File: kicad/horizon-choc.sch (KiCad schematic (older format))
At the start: 96 parts, among them J1 OLED, SW1 SW_Push, SW10 SW_Push, SW11 SW_Push, SW12 SW_Push, SW13 SW_Push, SW14 SW_Push, SW15 SW_Push, SW16 SW_Push, SW17 SW_Push, SW18 SW_Push, SW19 SW_Push, SW2 SW_Push, SW20 SW_Push, SW21 SW_Push, SW22 SW_Push, SW23 SW_Push, SW24 SW_Push, SW25 SW_Push, SW26 SW_Push, SW27 SW_Push, SW28 SW_Push, SW29 SW_Push, SW3 SW_Push, SW30 SW_Push, SW31 SW_Push, SW32 SW_Push, SW33 SW_Push, SW34 SW_Push, SW35 SW_Push, SW36 SW_Push, SW37 SW_Push, SW38 SW_Push, SW39 SW_Push, SW4 SW_Push, SW40 SW_Push, SW41 SW_Push, SW42 SW_Push, SW5 SW_Push, SW6 SW_Push, SW7 SW_Push, SW8 SW_Push, SW9 SW_Push, U1 PRO-MICRO

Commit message: Adjust center component layout for MX and Choc consistency.
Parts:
- SW1, SW10, SW11, SW12, SW13, SW14, SW15, SW16, SW17, SW18, SW19, SW2, SW20, SW21, SW22, SW23, SW24, SW25, SW26, SW27, SW28, SW29, SW3, SW30, SW31, SW32, SW33, SW34, SW35, SW36, SW37, SW38, SW39, SW4, SW40, SW41, SW42, SW5, SW6, SW7, SW8, SW9: footprint horizon-footprints:SW_MX -> horizon-footprints:SW_Choc

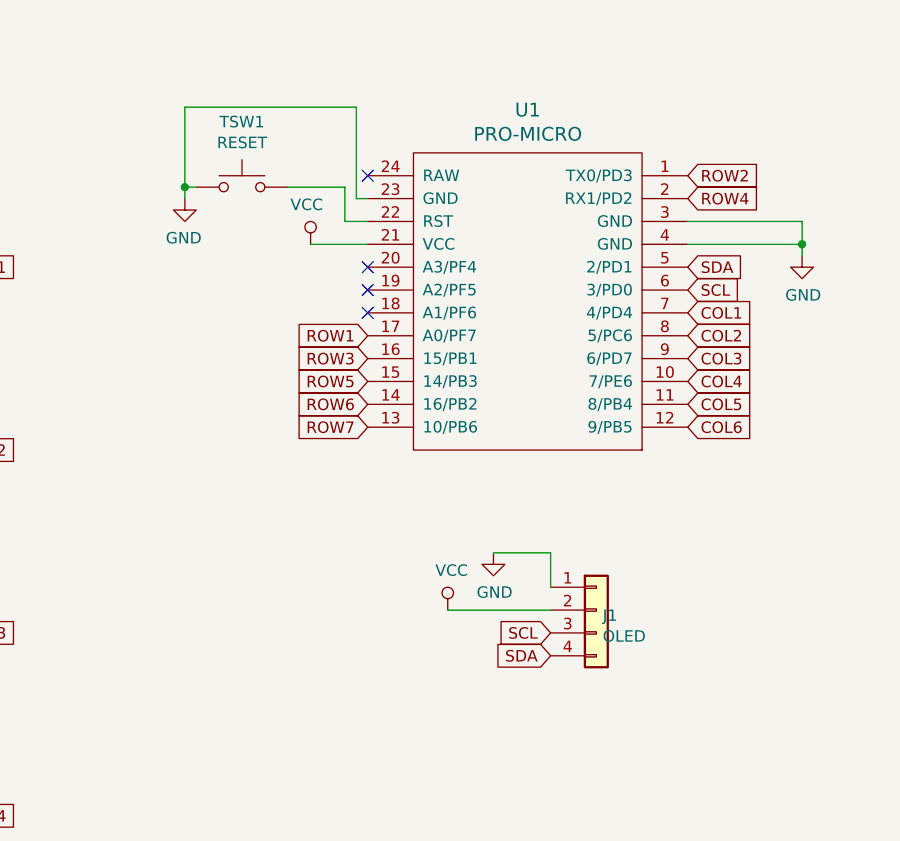
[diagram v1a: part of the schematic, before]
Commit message: Route traces on choc version
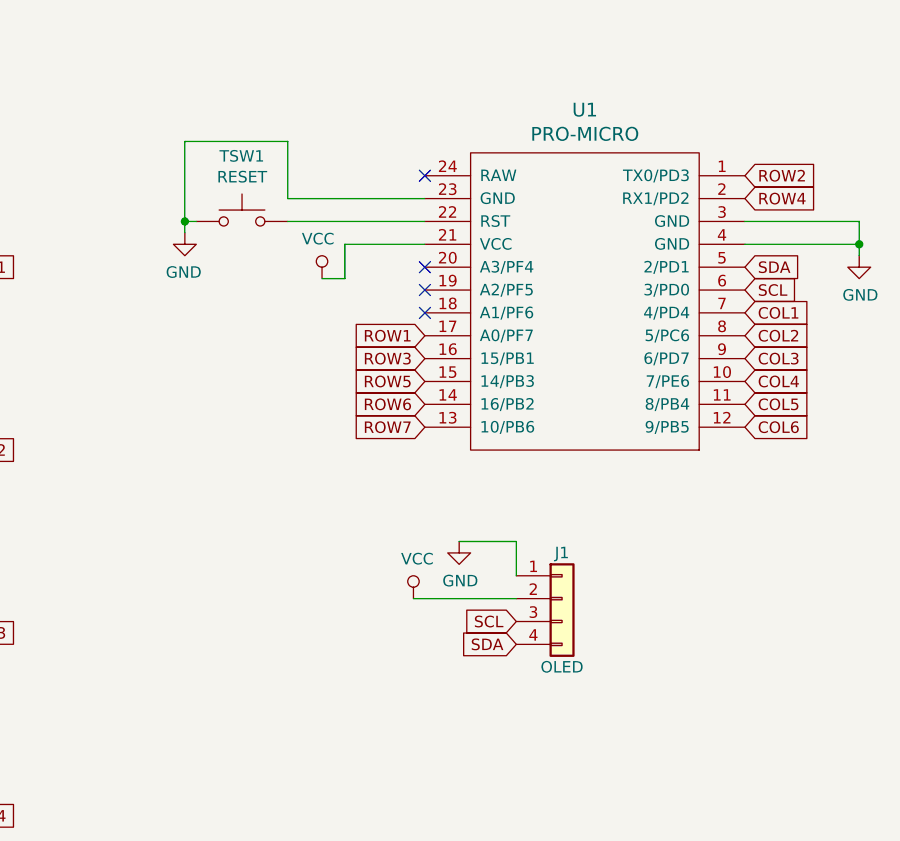
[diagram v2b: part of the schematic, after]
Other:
- moved on the sheet: J1, TSW1, U1
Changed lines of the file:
@@
 	1    0    0    -1
 $EndComp
-NoConn ~ 7800 1800
-Text GLabel 9200 2300 2    50   Input ~ 0
+NoConn ~ 8050 1800
+Text GLabel 9450 2300 2    50   Input ~ 0
 COL4
-Text GLabel 9200 1400 2    50   Input ~ 0
+Text GLabel 9450 1400 2    50   Input ~ 0
 ROW2
-Text GLabel 7800 2500 0    50   Input ~ 0
+Text GLabel 8050 2500 0    50   Input ~ 0
 ROW7
-Text GLabel 7800 2400 0    50   Input ~ 0
+Text GLabel 8050 2400 0    50   Input ~ 0
 ROW6
-Text GLabel 7800 2300 0    50   Input ~ 0
+Text GLabel 8050 2300 0    50   Input ~ 0
 ROW5
-Text GLabel 9200 1500 2    50   Input ~ 0
+Text GLabel 9450 1500 2    50   Input ~ 0
 ROW4
-Text GLabel 7800 2100 0    50   Input ~ 0
+Text GLabel 8050 2100 0    50   Input ~ 0
 ROW1
-Text GLabel 7800 2200 0    50   Input ~ 0
+Text GLabel 8050 2200 0    50   Input ~ 0
 ROW3
-Text GLabel 9200 2500 2    50   Input ~ 0
+Text GLabel 9450 2500 2    50   Input ~ 0
 COL6
-Text GLabel 9200 2400 2    50   Input ~ 0
+Text GLabel 9450 2400 2    50   Input ~ 0
 COL5
-Text GLabel 9200 2200 2    50   Input ~ 0
+Text GLabel 9450 2200 2    50   Input ~ 0
 COL3
-Text GLabel 9200 2100 2    50   Input ~ 0
+Text GLabel 9450 2100 2    50   Input ~ 0
 COL2
-Text GLabel 9200 2000 2    50   Input ~ 0
+Text GLabel 9450 2000 2    50   Input ~ 0
 COL1
 $Comp
 L horizon-components:Pro-Micro U1
 U 1 1 60FAFA60
-P 8500 1950
-F 0 "U1" H 8500 2787 60  0000 C CNN
-F 1 "PRO-MICRO" H 8500 2681 60  0000 C CNN
-F 2 "horizon-footprints:Pro-Micro" V 9550 -550 60  0001 C CNN
-F 3 "" V 9550 -550 60  0001 C CNN
-	1    8500 1950
+P 8750 1950
+F 0 "U1" H 8750 2787 60  0000 C CNN
+F 1 "PRO-MICRO" H 8750 2681 60  0000 C CNN
+F 2 "horizon-footprints:Pro-Micro" V 9800 -550 60  0001 C CNN
+F 3 "" V 9800 -550 60  0001 C CNN
+	1    8750 1950
 	-1   0    0    -1
 $EndComp
@@
 $EndComp
 NoConn ~ 9050 4550
-Text GLabel 8600 3500 0    50   Input ~ 0
+Text GLabel 8450 3450 0    50   Input ~ 0
 SDA
-Text GLabel 8600 3400 0    50   Input ~ 0
+Text GLabel 8450 3350 0    50   Input ~ 0
 SCL
 Wire Wire Line
-	8600 3050 8350 3050
-Wire Wire Line
-	8600 3200 8600 3050
-Wire Wire Line
-	8150 3300 8600 3300
+	8450 3000 8200 3000
+Wire Wire Line
+	8450 3150 8450 3000
+Wire Wire Line
+	8000 3250 8450 3250
 $Comp
 L power:VCC #PWR0105
 U 1 1 61061E80
-P 8150 3300
-F 0 "#PWR0105" H 8150 3150 50  0001 C CNN
-F 1 "VCC" H 8167 3473 50  0000 C CNN
-F 2 "" H 8150 3300 50  0001 C CNN
-F 3 "" H 8150 3300 50  0001 C CNN
-	1    8150 3300
-	1    0    0    -1
-$EndComp
-Wire Wire Line
-	7750 1100 7000 1100
-Wire Wire Line
-	7750 1100 7750 1500
-Wire Wire Line
-	7700 1600 7700 1450
-Wire Wire Line
-	7800 1600 7700 1600
-Wire Wire Line
-	7800 1700 7550 1700
+P 8000 3250
+F 0 "#PWR0105" H 8000 3100 50  0001 C CNN
+F 1 "VCC" H 8017 3423 50  0000 C CNN
+F 2 "" H 8000 3250 50  0001 C CNN
+F 3 "" H 8000 3250 50  0001 C CNN
+	1    8000 3250
+	1    0    0    -1
+$EndComp
+Text GLabel 9450 1900 2    50   Input ~ 0
+SCL
+Text GLabel 9450 1800 2    50   Input ~ 0
+SDA
+$Comp
+L power:GND #PWR0103
+U 1 1 6102AE0C
+P 8200 3000
+F 0 "#PWR0103" H 8200 2750 50  0001 C CNN
+F 1 "GND" H 8205 2827 50  0000 C CNN
+F 2 "" H 8200 3000 50  0001 C CNN
+F 3 "" H 8200 3000 50  0001 C CNN
+	1    8200 3000
+	1    0    0    -1
+$EndComp
+Connection ~ 7000 1600
+Wire Wire Line
+	7000 1250 7000 1600
+Wire Wire Line
+	7000 1600 7000 1650
+Wire Wire Line
+	7050 1600 7000 1600
+$Comp
+L horizon-components:SW_Push TSW1
+U 1 1 60FA8D3C
+P 7250 1600
+F 0 "TSW1" H 7250 1885 50  0000 C CNN
+F 1 "RESET" H 7250 1794 50  0000 C CNN
+F 2 "horizon-footprints:SW_Push_6mm" H 7250 1800 50  0001 C CNN
+F 3 "~" H 7250 1800 50  0001 C CNN
+	1    7250 1600
+	-1   0    0    -1
+$EndComp
+Connection ~ 9950 1700
+Wire Wire Line
+	9950 1600 9950 1700
+Wire Wire Line
+	9450 1600 9950 1600
+Wire Wire Line
+	9950 1700 9950 1750
+Wire Wire Line
+	9450 1700 9950 1700
+$Comp
+L power:GND #PWR0102
+U 1 1 60FC2164
+P 9950 1750
+F 0 "#PWR0102" H 9950 1500 50  0001 C CNN
+F 1 "GND" H 9955 1577 50  0000 C CNN
+F 2 "" H 9950 1750 50  0001 C CNN
+F 3 "" H 9950 1750 50  0001 C CNN
+	1    9950 1750
+	1    0    0    -1
+$EndComp
+$Comp
+L power:GND #PWR0101
+U 1 1 60FB8E05
+P 7000 1650
+F 0 "#PWR0101" H 7000 1400 50  0001 C CNN
+F 1 "GND" H 7005 1477 50  0000 C CNN
+F 2 "" H 7000 1650 50  0001 C CNN
+F 3 "" H 7000 1650 50  0001 C CNN
+	1    7000 1650
+	-1   0    0    -1
+$EndComp
+NoConn ~ 8050 1900
+NoConn ~ 8050 2000
 $Comp
 L power:VCC #PWR0104
 U 1 1 610375EA
-P 7550 1700
-F 0 "#PWR0104" H 7550 1550 50  0001 C CNN
-F 1 "VCC" H 7567 1873 50  0000 C CNN
-F 2 "" H 7550 1700 50  0001 C CNN
-F 3 "" H 7550 1700 50  0001 C CNN
-	1    7550 1700
-	-1   0    0    -1
-$EndComp
-Text GLabel 9200 1900 2    50   Input ~ 0
-SCL
-Text GLabel 9200 1800 2    50   Input ~ 0
-SDA
-$Comp
-L power:GND #PWR0103
-U 1 1 6102AE0C
-P 8350 3050
-F 0 "#PWR0103" H 8350 2800 50  0001 C CNN
-F 1 "GND" H 8355 2877 50  0000 C CNN
-F 2 "" H 8350 3050 50  0001 C CNN
-F 3 "" H 8350 3050 50  0001 C CNN
-	1    8350 3050
-	1    0    0    -1
-$EndComp
+P 7600 1850
+F 0 "#PWR0104" H 7600 1700 50  0001 C CNN
+F 1 "VCC" H 7617 2023 50  0000 C CNN
+F 2 "" H 7600 1850 50  0001 C CNN
+F 3 "" H 7600 1850 50  0001 C CNN
+	1    7600 1850
+	-1   0    0    -1
+$EndComp
+Wire Wire Line
+	7450 1500 7450 1250
+Wire Wire Line
+	7450 1250 7000 1250
+Wire Wire Line
+	8050 1700 7700 1700
+Wire Wire Line
+	7700 1700 7700 1850
+Wire Wire Line
+	7700 1850 7600 1850
+Wire Wire Line
+	8050 1600 7450 1600
+Wire Wire Line
+	8050 1500 7450 1500
 $Comp
 L horizon-components:Conn_01x04 J1
 U 1 1 6102700A
-P 8800 3300
-F 0 "J1" H 8828 3276 50  0000 L CNN
-F 1 "OLED" H 8828 3185 50  0000 L CNN
-F 2 "horizon-footprints:Header_1x04_2.54mm" H 8800 3300 50  0001 C CNN
-F 3 "~" H 8800 3300 50  0001 C CNN
-	1    8800 3300
-	1    0    0    -1
-$EndComp
-Connection ~ 7000 1450
-Wire Wire Line
-	7000 1100 7000 1450
-Wire Wire Line
-	7800 1500 7750 1500
-Wire Wire Line
-	7000 1450 7000 1500
-Wire Wire Line
-	7050 1450 7000 1450
-Wire Wire Line
-	7700 1450 7450 1450
-$Comp
-L horizon-components:SW_Push TSW1
-U 1 1 60FA8D3C
-P 7250 1450
-F 0 "TSW1" H 7250 1735 50  0000 C CNN
-F 1 "RESET" H 7250 1644 50  0000 C CNN
-F 2 "horizon-footprints:SW_Push_6mm" H 7250 1650 50  0001 C CNN
-F 3 "~" H 7250 1650 50  0001 C CNN
-	1    7250 1450
-	-1   0    0    -1
-$EndComp
-NoConn ~ 7800 1400
-Connection ~ 9700 1700
-Wire Wire Line
-	9700 1600 9700 1700
-Wire Wire Line
-	9200 1600 9700 1600
-Wire Wire Line
-	9700 1700 9700 1750
-Wire Wire Line
-	9200 1700 9700 1700
-$Comp
-L power:GND #PWR0102
-U 1 1 60FC2164
-P 9700 1750
-F 0 "#PWR0102" H 9700 1500 50  0001 C CNN
-F 1 "GND" H 9705 1577 50  0000 C CNN
-F 2 "" H 9700 1750 50  0001 C CNN
-F 3 "" H 9700 1750 50  0001 C CNN
-	1    9700 1750
-	1    0    0    -1
-$EndComp
-$Comp
-L power:GND #PWR0101
-U 1 1 60FB8E05
-P 7000 1500
-F 0 "#PWR0101" H 7000 1250 50  0001 C CNN
-F 1 "GND" H 7005 1327 50  0000 C CNN
-F 2 "" H 7000 1500 50  0001 C CNN
-F 3 "" H 7000 1500 50  0001 C CNN
-	1    7000 1500
-	-1   0    0    -1
-$EndComp
-NoConn ~ 7800 1900
-NoConn ~ 7800 2000
+P 8650 3250
+F 0 "J1" H 8650 3450 50  0000 C CNN
+F 1 "OLED" H 8650 2950 50  0000 C CNN
+F 2 "horizon-footprints:Header_1x04_2.54mm" H 8650 3250 50  0001 C CNN
+F 3 "~" H 8650 3250 50  0001 C CNN
+	1    8650 3250
+	1    0    0    -1
+$EndComp
+NoConn ~ 8050 1400
 $EndSCHEMATC

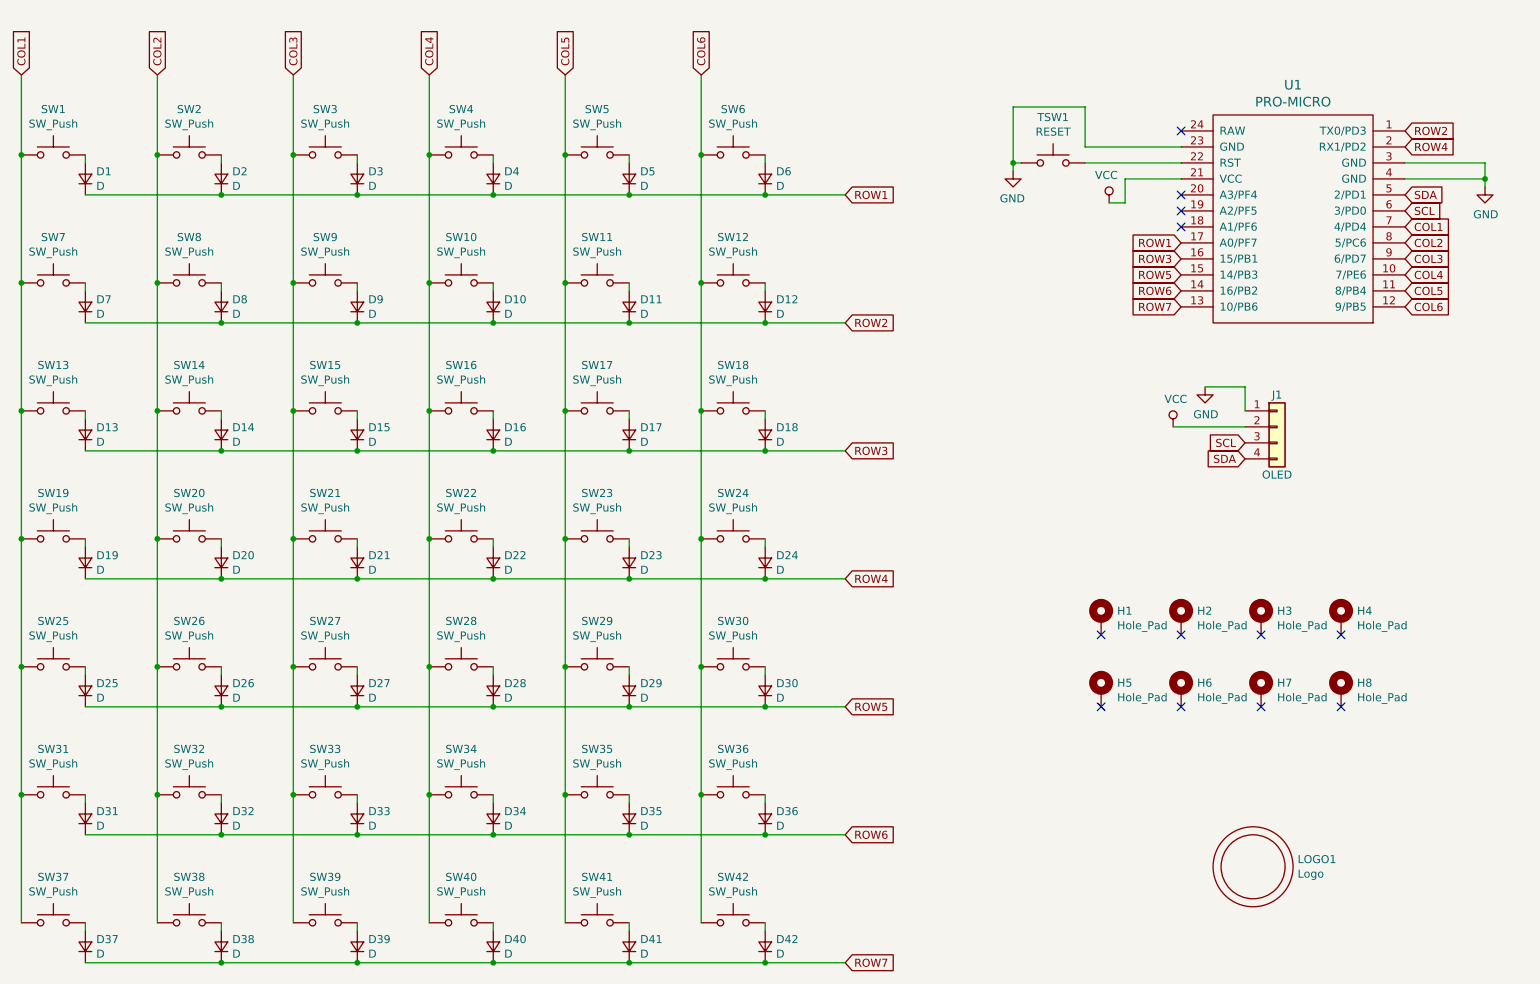
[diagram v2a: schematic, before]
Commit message: Implement battery on Choc version, plus bottom and top PCBs
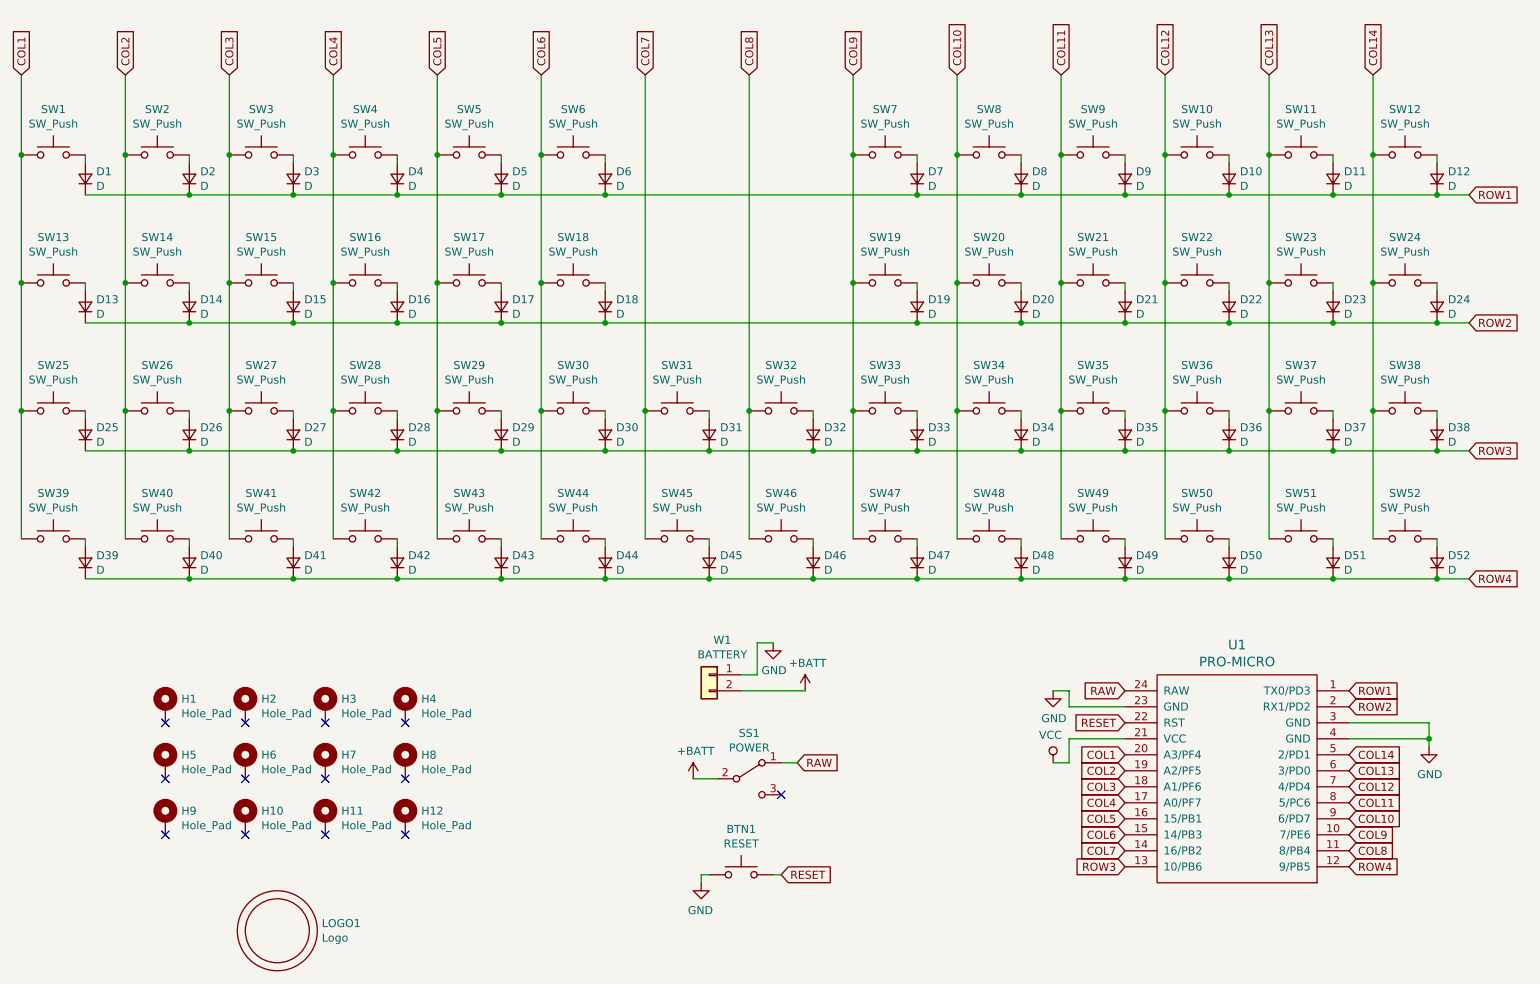
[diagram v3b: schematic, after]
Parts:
- removed D25, D39: D, horizon-footprints:D_SOD-123, symbol horizon-components:D
- removed J1: OLED, horizon-footprints:Header_1x04_2.54mm, symbol horizon-components:Conn_01x04
- removed SW25, SW39: SW_Push, horizon-footprints:SW_Choc, symbol horizon-components:SW_Push
- added D19, D43, D44, D45, D46, D47, D48, D49, D50, D51, D52, D7: D, horizon-footprints:D_SOD-123, symbol horizon-components:D
- added H10, H11, H12, H9: Hole_Pad, horizon-footprints:Mount_M2, symbol horizon-components:Hole_Pad
- added SS1: POWER, horizon-footprints:SS12D00, symbol horizon-components:SW_SPDT
- added SW19, SW43, SW44, SW45, SW46, SW47, SW48, SW49, SW50, SW51, SW52, SW7: SW_Push, horizon-footprints:SW_Choc, symbol horizon-components:SW_Push
- added W1: BATTERY, horizon-footprints:Battery_Wire_Pads, symbol horizon-components:Conn_01x02
- renumbered TSW1 to BTN1, D7 to D13, D13 to D25, D19 to D39, SW7 to SW13, SW13 to SW25, SW19 to SW39
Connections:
- net COL1: now also U1.20 (A3/PF4); no longer SW31.1, SW37.1, U1.7 (4/PD4)
- net COL2: now also SW40.1, U1.19 (A2/PF5); no longer SW20.1, SW32.1, SW38.1, SW8.1, U1.8 (5/PC6)
- net COL3: now also SW41.1, U1.18 (A1/PF6); no longer SW21.1, SW33.1, SW9.1, U1.9 (6/PD7)
- net COL4: now also SW42.1, U1.17 (A0/PF7); no longer SW10.1, SW22.1, SW34.1, SW40.1, U1.10 (7/PE6)
- net COL5: now also U1.16 (15/PB1), SW43.1; no longer SW11.1, SW23.1, SW35.1, SW41.1, U1.11 (8/PB4)
- net COL6: now also U1.15 (14/PB3), SW44.1; no longer SW12.1, SW24.1, SW36.1, SW42.1, U1.12 (9/PB5)
- net GND: now also W1.1 (Pin_1)
- net ROW1: now also D10.1 (K), D11.1 (K), D12.1 (K), D8.1 (K), D9.1 (K), U1.1 (TX0/PD3), D7.1 (K); no longer U1.17 (A0/PF7)
- net ROW2: now also D14.1 (K), D15.1 (K), D16.1 (K), D17.1 (K), D18.1 (K), D20.1 (K), D21.1 (K), D22.1 (K), D23.1 (K), D24.1 (K), U1.2 (RX1/PD2), D19.1 (K); no longer D10.1 (K), D11.1 (K), D12.1 (K), D8.1 (K), D9.1 (K), U1.1 (TX0/PD3)
- net ROW3: now also D26.1 (K), D27.1 (K), D28.1 (K), D29.1 (K), D30.1 (K), D31.1 (K), D32.1 (K), D33.1 (K), D34.1 (K), D35.1 (K), D36.1 (K), D37.1 (K), D38.1 (K), U1.13 (10/PB6); no longer D14.1 (K), D15.1 (K), D16.1 (K), D17.1 (K), D18.1 (K), U1.16 (15/PB1)
- net ROW4: now also D40.1 (K), D41.1 (K), D42.1 (K), U1.12 (9/PB5), D43.1 (K), D44.1 (K), D45.1 (K), D46.1 (K), D47.1 (K), D48.1 (K), D49.1 (K), D50.1 (K), D51.1 (K), D52.1 (K); no longer D20.1 (K), D21.1 (K), D22.1 (K), D23.1 (K), D24.1 (K), U1.2 (RX1/PD2)
- net RESET: now reaches BTN1.1, U1.22 (RST)
- net RAW: now reaches U1.24 (RAW)
- net RAW: now also SS1.1 (A)
- removed net ROW5: D26.1 (K), D27.1 (K), D28.1 (K), D29.1 (K), D30.1 (K), U1.15 (14/PB3)
- removed net ROW6: D31.1 (K), D32.1 (K), D33.1 (K), D34.1 (K), D35.1 (K), D36.1 (K), U1.14 (16/PB2)
- removed net ROW7: D37.1 (K), D38.1 (K), D40.1 (K), D41.1 (K), D42.1 (K), U1.13 (10/PB6)
- net SCL renamed COL13
- net COL13: now also SW11.1, SW23.1, SW37.1, SW51.1
- net SDA renamed COL14
- net COL14: now also SW12.1, SW24.1, SW38.1, SW52.1
- new net: D43.2 (A), SW43.2
- new net: D44.2 (A), SW44.2
- new net: D45.2 (A), SW45.2
- new net: D46.2 (A), SW46.2
- new net: D7.2 (A), SW7.2
- new net: D19.2 (A), SW19.2
- new net: D47.2 (A), SW47.2
- new net: D48.2 (A), SW48.2
- new net: D49.2 (A), SW49.2
- new net: D50.2 (A), SW50.2
- new net: D51.2 (A), SW51.2
- new net: D52.2 (A), SW52.2
- new net +BATT: SS1.2 (B), W1.2 (Pin_2)
- new net COL10: SW20.1, SW34.1, SW48.1, SW8.1, U1.9 (6/PD7)
- new net COL11: SW21.1, SW35.1, SW49.1, SW9.1, U1.8 (5/PC6)
- new net COL12: SW10.1, SW22.1, SW36.1, SW50.1, U1.7 (4/PD4)
- new net COL7: SW31.1, SW45.1, U1.14 (16/PB2)
- new net COL8: SW32.1, SW46.1, U1.11 (8/PB4)
- new net COL9: SW19.1, SW33.1, SW47.1, SW7.1, U1.10 (7/PE6)
- no-connect marks 12 -> 13
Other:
- moved on the sheet: BTN1, H1, H2, H3, H4, LOGO1, U1
